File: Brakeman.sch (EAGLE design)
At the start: 9 parts

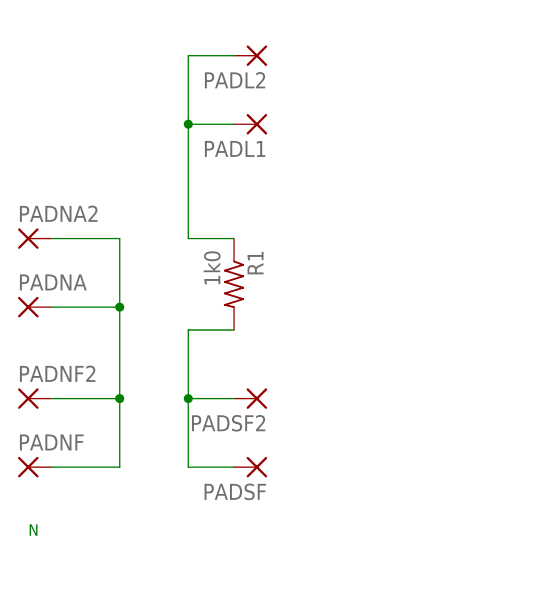
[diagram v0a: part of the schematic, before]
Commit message: added values for connectors
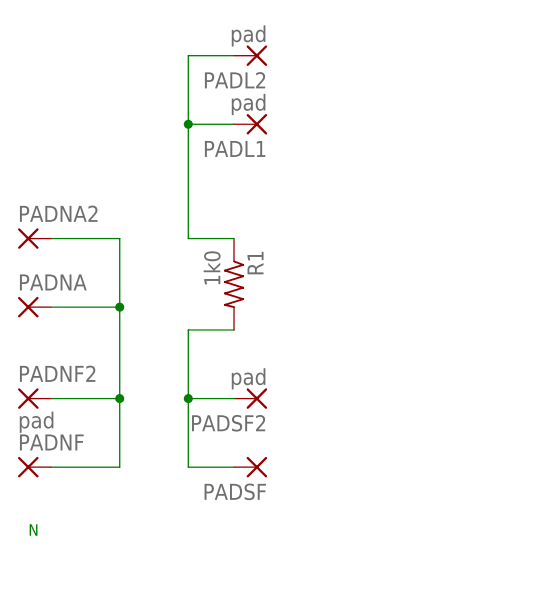
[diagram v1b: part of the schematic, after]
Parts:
- PADL1, PADL2, PADNF2, PADSF2: value (none) -> pad
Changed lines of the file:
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@@
 <part name="FRAME1" library="SparkFun" deviceset="FRAME-LETTER" device=""/>
 <part name="R1" library="resistor" deviceset="R-US_" device="0204/5" value="1k0"/>
-<part name="PADNF2" library="wirepad" deviceset="SMD2" device=""/>
+<part name="PADNF2" library="wirepad" deviceset="SMD2" device="" value="pad"/>
 <part name="PADSF" library="wirepad" deviceset="SMD2" device=""/>
 <part name="PADNF" library="wirepad" deviceset="SMD2" device=""/>
-<part name="PADSF2" library="wirepad" deviceset="SMD2" device=""/>
-<part name="PADL1" library="wirepad" deviceset="SMD2" device=""/>
+<part name="PADSF2" library="wirepad" deviceset="SMD2" device="" value="pad"/>
+<part name="PADL1" library="wirepad" deviceset="SMD2" device="" value="pad"/>
 <part name="PADNA" library="wirepad" deviceset="SMD2" device=""/>
 <part name="PADNA2" library="wirepad" deviceset="SMD2" device=""/>
-<part name="PADL2" library="wirepad" deviceset="SMD2" device=""/>
+<part name="PADL2" library="wirepad" deviceset="SMD2" device="" value="pad"/>
 </parts>
 <sheets>

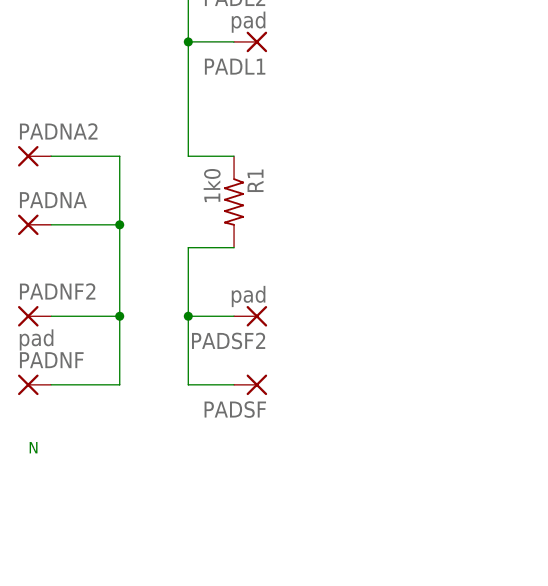
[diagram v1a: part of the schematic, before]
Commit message: added values for connectors
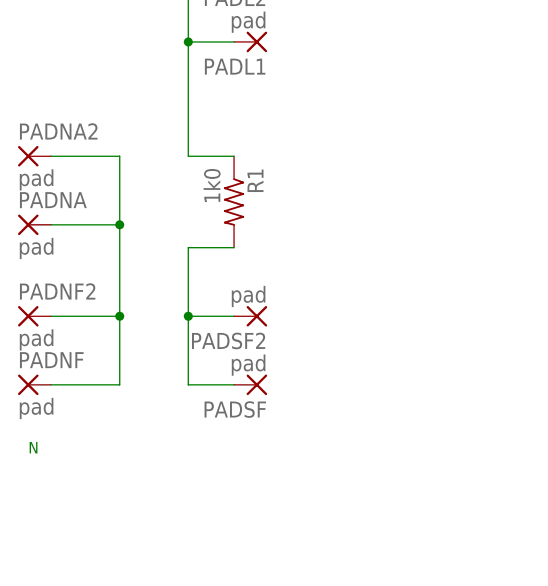
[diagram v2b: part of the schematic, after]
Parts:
- PADNA, PADNA2, PADNF, PADSF: value (none) -> pad
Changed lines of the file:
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@@
 <part name="R1" library="resistor" deviceset="R-US_" device="0204/5" value="1k0"/>
 <part name="PADNF2" library="wirepad" deviceset="SMD2" device="" value="pad"/>
-<part name="PADSF" library="wirepad" deviceset="SMD2" device=""/>
-<part name="PADNF" library="wirepad" deviceset="SMD2" device=""/>
+<part name="PADSF" library="wirepad" deviceset="SMD2" device="" value="pad"/>
+<part name="PADNF" library="wirepad" deviceset="SMD2" device="" value="pad"/>
 <part name="PADSF2" library="wirepad" deviceset="SMD2" device="" value="pad"/>
 <part name="PADL1" library="wirepad" deviceset="SMD2" device="" value="pad"/>
-<part name="PADNA" library="wirepad" deviceset="SMD2" device=""/>
-<part name="PADNA2" library="wirepad" deviceset="SMD2" device=""/>
+<part name="PADNA" library="wirepad" deviceset="SMD2" device="" value="pad"/>
+<part name="PADNA2" library="wirepad" deviceset="SMD2" device="" value="pad"/>
 <part name="PADL2" library="wirepad" deviceset="SMD2" device="" value="pad"/>
 </parts>

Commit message: Version 2.4
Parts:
- removed PADL1, PADL2, PADNA, PADNA2, PADNF2, PADSF2: pad, wirepad:SMD2
- removed R1: 1k0, resistor:R-US_0204/5
- added LED1, LED2: (no value), SPCoast:LED0603-LED
- added PADNF1, PADSF1: pad, SPCoast:SMD2
- added R1K: 1k0, resistor:R-US_R0603
- PADNF, PADSF: device wirepad:SMD2 -> SPCoast:SMD2
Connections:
- net LIMITED: now also LED1.C, LED2.A, R1K.1; no longer PADL1.P, PADL2.P, R1.1
- net N: now also LED1.A, LED2.C, PADNF1.P; no longer PADNA.P, PADNA2.P, PADNF2.P
- net S: now also PADSF1.P, R1K.2; no longer PADSF2.P, R1.2

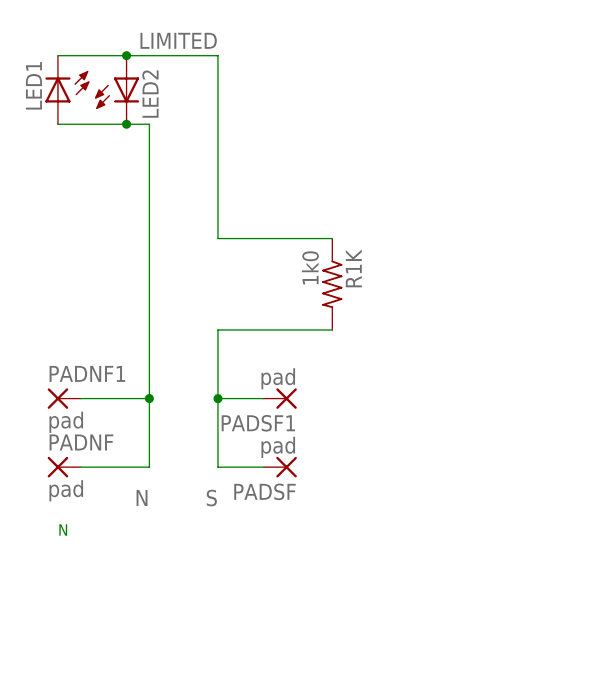
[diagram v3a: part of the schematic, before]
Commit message: Revert "Version 2.4"
This reverts commit de817f9b6bc09cb4258c25781ce6263bd1cc7bce.
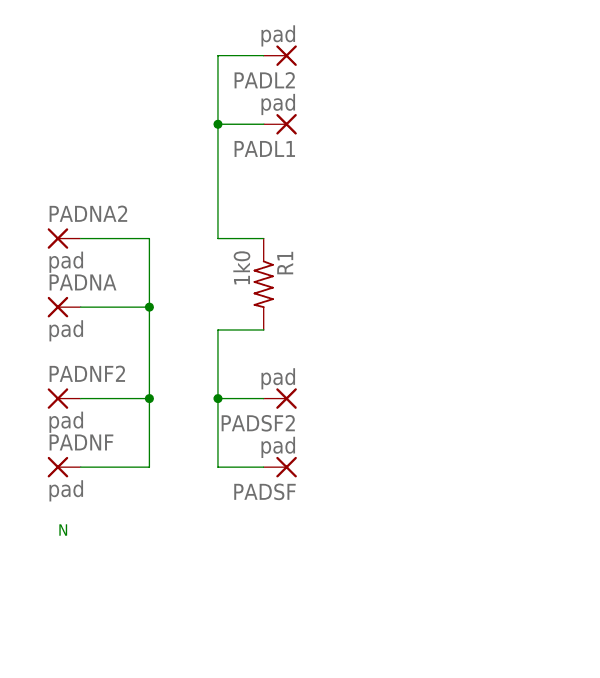
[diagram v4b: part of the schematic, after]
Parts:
- removed LED1, LED2: (no value), SPCoast:LED0603-LED
- removed PADNF1, PADSF1: pad, SPCoast:SMD2
- removed R1K: 1k0, resistor:R-US_R0603
- added PADL1, PADL2, PADNA, PADNA2, PADNF2, PADSF2: pad, wirepad:SMD2
- added R1: 1k0, resistor:R-US_0204/5
- PADNF, PADSF: device SPCoast:SMD2 -> wirepad:SMD2
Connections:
- net LIMITED: now also PADL1.P, PADL2.P, R1.1; no longer LED1.C, LED2.A, R1K.1
- net N: now also PADNA.P, PADNA2.P, PADNF2.P; no longer LED1.A, LED2.C, PADNF1.P
- net S: now also PADSF2.P, R1.2; no longer PADSF1.P, R1K.2
